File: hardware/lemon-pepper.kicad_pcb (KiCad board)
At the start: 4 copper layers, 35 x 35 mm, 90 parts, among them J101 INPUT, J201 USB_C_Receptacle_USB2.0, J301 TagConnect, J302 USER CONN., M101 MOT, Q501 MMBT5551, SW301 USER, U201 SRV05-4, U301 STM32G431, U302 SN65HVD230, U401 MT6835, U501 MAX15062CATA+T, U601 L6226QTR, U701 MAX49925, U703 MAX49925, Y301 12MHz

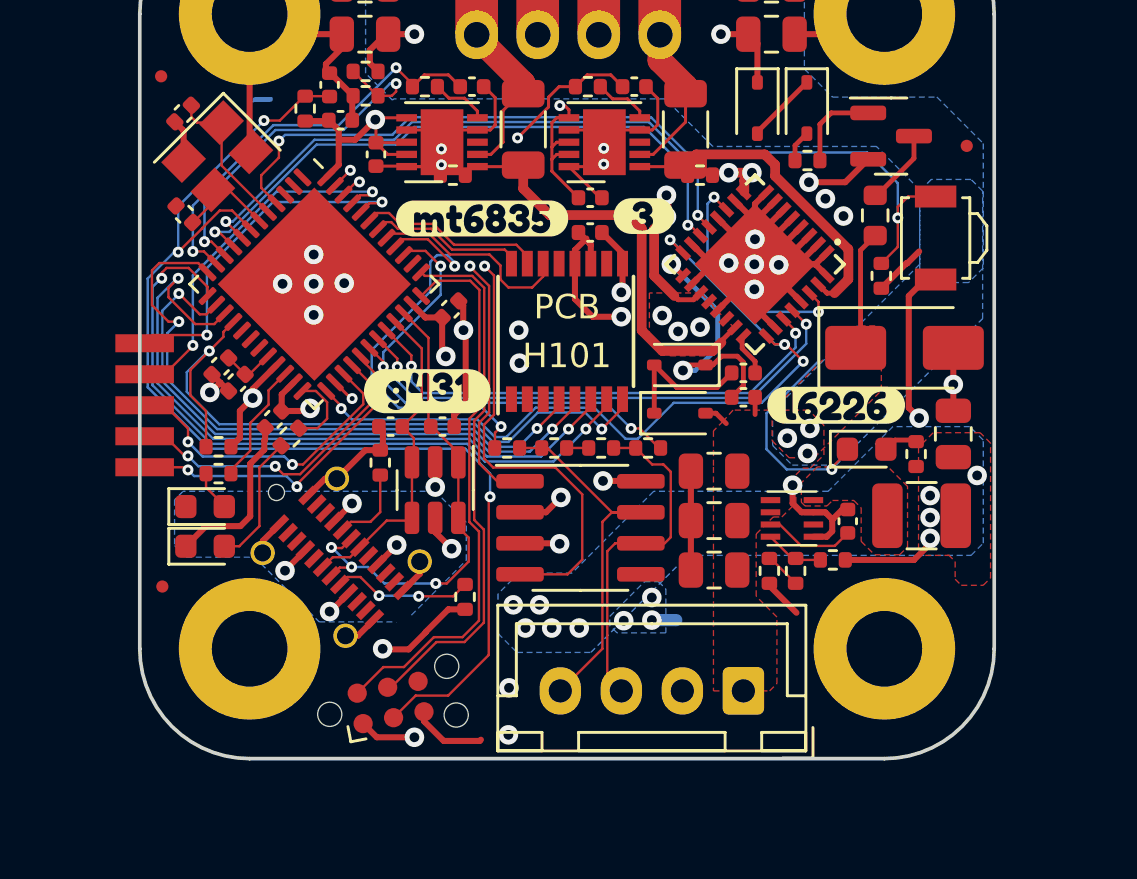
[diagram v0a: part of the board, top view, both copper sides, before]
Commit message: change inductor footprint, add I2C1 SCL on user 3
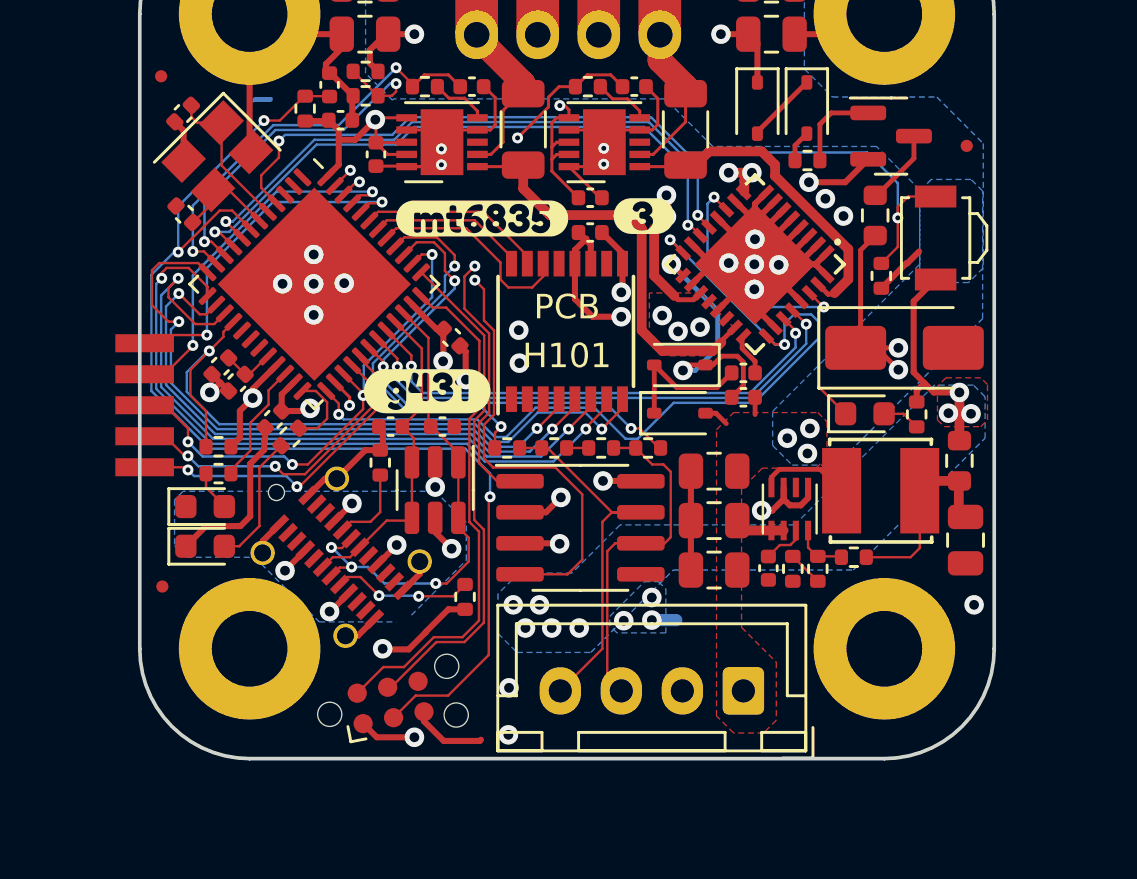
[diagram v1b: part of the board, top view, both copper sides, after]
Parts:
- removed the R701 at (141.6, 80.6)
- removed the R702 at (151.8, 80.6)
- removed kibuzzard-65305A5A: G***, kibuzzard-65305A5A
- added R506: 0R, Resistor_SMD:R_0603_1608Metric, F.Cu at (162.4, 92.3)
- L501: footprint Inductor_SMD:L_1210_3225Metric -> easyeda2kicad:IND-SMD_L4.0-W4.0
- R501: value 200k -> 0R
- U501: value MAX15062CATA+T -> MAX15062AATA+T
- moved C503 4.38 mm to (162.6, 95.5), turned to -90 degrees
- moved C502 3.78 mm to (154.6, 96.7), turned to -90 degrees
- moved L501 1.96 mm to (159.2, 93.5)
- moved R601 1.63 mm to (160.6, 90.4), turned to 90 degrees
- moved D601 1.45 mm to (158.5, 90.3)
- moved C304 1.16 mm to (141.6, 87.2), turned to -45 degrees
- moved R503 0.96 mm to (155.6, 96.7)
- moved R502 0.91 mm to (156.6, 96.7)
- moved R501 0.87 mm to (158.1, 96.2)
- moved U501 0.40 mm to (155.4, 94.2), turned to 0 degrees
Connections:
- net Net-(U301-PB10) renamed /mcu/LED_GOOD
- net Net-(U301-PB11) renamed /mcu/LED_FAULT
- C503 pad 1: +3V3 -> Net-(C503-Pad1)
- L501 pad 2: +3V3 -> Net-(C503-Pad1)
- R501 pad 1: +3V3 -> Net-(C503-Pad1)
- U301 pad 17: /current sense/W_SENSE -> unconnected-(U301-PB0-Pad17)
- U301 pad 38: unconnected-(U301-PA15-Pad38) -> /mcu/USER_3
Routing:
- net +3V3: track 66.8 -> 77.6 mm, vias 18 -> 16
- net GND: track 128.7 -> 118.9 mm
- net Net-(C503-Pad1): track 0.00 -> 8.09 mm
- net /mcu/USER_3: track 12.9 -> 20.9 mm, vias 2 -> 4
- net Vmot: track 18.6 -> 24.9 mm, vias 12 -> 14
- net Net-(D601-K): track 20.6 -> 15.0 mm, vias 3 -> 2
- net Net-(U501-LX): track 0.00 -> 3.79 mm
- net /half bridges/ENA: track 31.9 -> 35.3 mm, vias 4 -> 3
- net Net-(U501-VCC): track 3.75 -> 1.78 mm
- net /mcu/SWDIO: track 22.9 -> 21.2 mm
- net /mcu/DIR: track 21.0 -> 22.2 mm
- net /mcu/SWCLK: track 21.9 -> 20.8 mm
- net /mcu/STEP: track 17.3 -> 16.4 mm
- net /mcu/CAN_RX: track 26.3 -> 27.0 mm
- removed copper zone on F.Cu, net Net-(U501-LX)

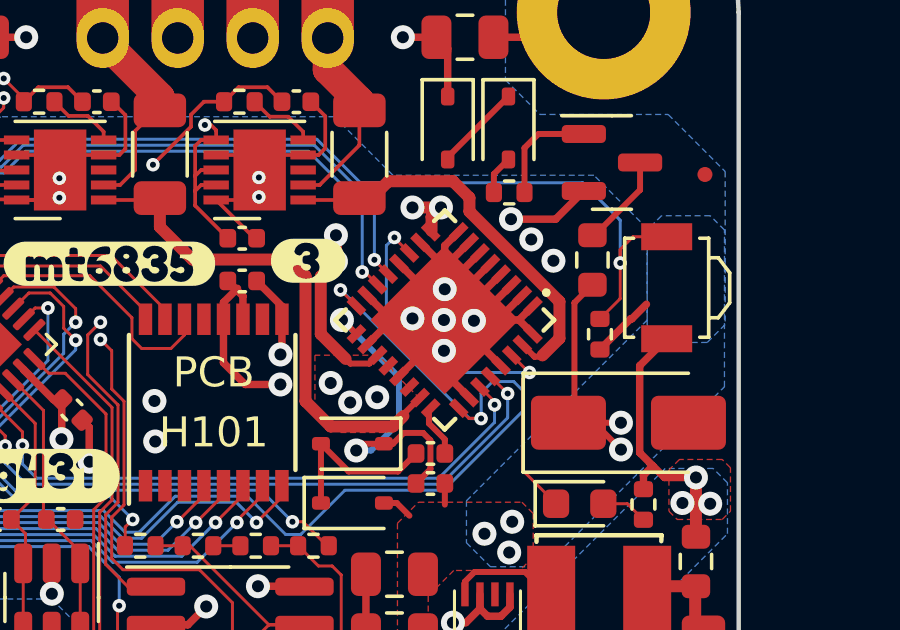
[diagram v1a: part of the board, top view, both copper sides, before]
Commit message: update L6226Q footprint and symbol
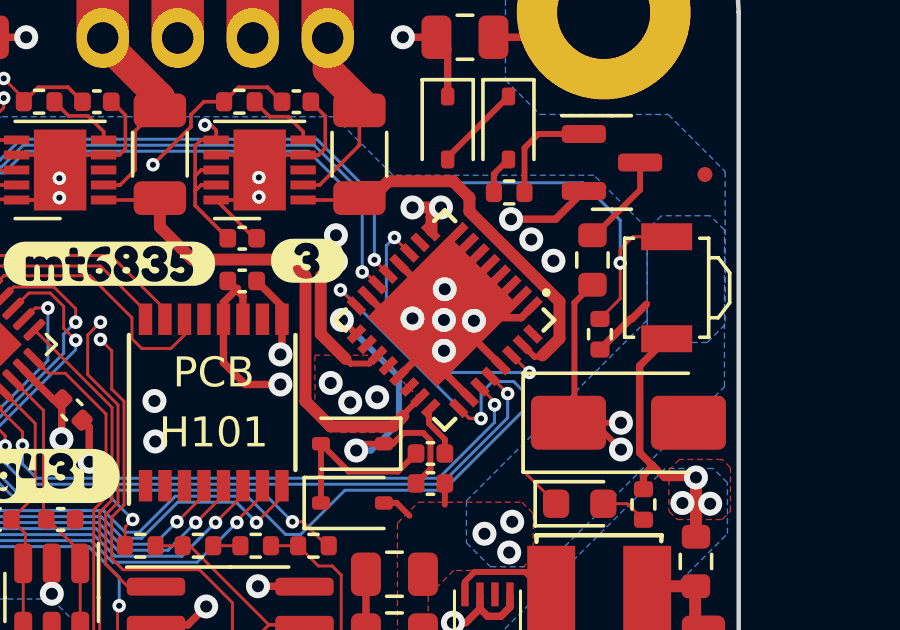
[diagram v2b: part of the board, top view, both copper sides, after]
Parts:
- U601: footprint easyeda2kicad:VQFN-32_L5.0-W5.0-P0.50-TL-EP -> matei:ST-L6226Q-VQFN32
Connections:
- U601 pad 10: GND -> unconnected-(U601-NC-Pad10)
- U601 pad 18: GND -> unconnected-(U601-NC-Pad18)
- U601 pad 32: GND -> unconnected-(U601-NC-Pad32)
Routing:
- net GND: track 118.9 -> 115.9 mm
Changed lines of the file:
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@@
   (net 86 "Net-(U703-OUT)")
   (net 87 "Net-(C503-Pad1)")
+  (net 88 "unconnected-(U601-NC-Pad10)")
+  (net 89 "unconnected-(U601-NC-Pad18)")
+  (net 90 "unconnected-(U601-NC-Pad32)")
   (footprint "Capacitor_SMD:C_0805_2012Metric" (layer "F.Cu")
     (at 138.025 74.8)
@@
     )
   )
-  (footprint "easyeda2kicad:VQFN-32_L5.0-W5.0-P0.50-TL-EP" (layer "F.Cu")
+  (footprint "matei:ST-L6226Q-VQFN32" (layer "F.Cu")
     (at 154 84.225 -135)
     (property "LCSC Part" "C95357")
@@
       (stroke (width 0.06) (type solid)) (fill none) (layer "F.Fab"))
     (pad "1" smd rect (at -2.41 -1.75 225) (size 0.66 0.28) (layers "F.Cu" "F.Paste" "F.Mask")
-      (net 1 "GND") (pinfunction "GND") (pintype "power_out"))
+      (net 1 "GND") (pinfunction "GND") (pintype "power_in"))
     (pad "2" smd rect (at -2.41 -1.25 225) (size 0.66 0.28) (layers "F.Cu" "F.Paste" "F.Mask")
       (net 1 "GND") (pinfunction "NC") (pintype "passive"))
@@
       (net 75 "/half bridges/OUT1B") (pinfunction "OUT1B") (pintype "output"))
     (pad "10" smd rect (at -1.25 2.41 225) (size 0.28 0.66) (layers "F.Cu" "F.Paste" "F.Mask")
-      (net 1 "GND") (pinfunction "NC") (pintype "passive"))
+      (net 88 "unconnected-(U601-NC-Pad10)") (pinfunction "NC") (pintype "no_connect"))
     (pad "11" smd rect (at -0.75 2.41 225) (size 0.28 0.66) (layers "F.Cu" "F.Paste" "F.Mask")
       (net 31 "Net-(D601-K)") (pinfunction "OCDB") (pintype "open_emitter"))
@@
       (net 30 "Net-(D603-K)") (pinfunction "VBOOT") (pintype "passive"))
     (pad "18" smd rect (at 2.41 1.25 225) (size 0.66 0.28) (layers "F.Cu" "F.Paste" "F.Mask")
-      (net 1 "GND") (pinfunction "NC") (pintype "passive"))
+      (net 89 "unconnected-(U601-NC-Pad18)") (pinfunction "NC") (pintype "no_connect"))
     (pad "19" smd rect (at 2.41 0.75 225) (size 0.66 0.28) (layers "F.Cu" "F.Paste" "F.Mask")
       (net 11 "/current sense/W_IN") (pinfunction "OUT2B") (pintype "output"))
@@
       (net 10 "/current sense/V_IN") (pinfunction "OUT1A") (pintype "output"))
     (pad "32" smd rect (at -1.75 -2.41 225) (size 0.28 0.66) (layers "F.Cu" "F.Paste" "F.Mask")
-      (net 1 "GND") (pinfunction "NC") (pintype "passive"))
-    (pad "33" smd rect (at 0 0 225) (size 3.5 3.5) (layers "F.Cu" "F.Paste" "F.Mask")
+      (net 90 "unconnected-(U601-NC-Pad32)") (pinfunction "NC") (pintype "no_connect"))
+    (pad "33" smd rect (at -0.165 0.25 225) (size 3.83 3.28) (layers "F.Cu" "F.Paste" "F.Mask")
       (net 1 "GND") (pinfunction "EP") (pintype "passive"))
     (model "/Users/mateijordache/Documents/KiCad/easyeda2kicad/easyeda2kicad.3dshapes/VQFN-32_L5.0-W5.0-H1.0-P0.50.wrl" hide
@@
     (pad "1" thru_hole circle locked (at 13 13) (size 5.8 5.8) (drill 3.1) (layers "*.Cu" "*.Mask")
       (net 1 "GND") (pinfunction "1") (pintype "input"))
-    (model "/Users/mateijordache/Documents/electronics_projects/lemon-pepper-stepper/mechanical/heatsink-nema-14.step" hide
-      (offset (xyz 0 0 0))
+    (model "/Users/mateijordache/Documents/electronics_projects/lemon-pepper-stepper/mechanical/heatsink-nema-14.step"
+      (offset (xyz 0 0 -1.5))
       (scale (xyz 1 1 1))
       (rotate (xyz 0 0 0))
@@
     (effects (font (size 1 1) (thickness 0.15)) (justify left bottom))
   )
+  (segment (start 156.549874 84.15) (end 155.55 84.15) (width 0.25) (layer "F.Cu") (net 1))
   (segment (start 152.575 84.225) (end 153.975 84.225) (width 0.25) (layer "F.Cu") (net 1))
   (segment (start 133.3 79.569365) (end 133.3 73.975) (width 0.25) (layer "F.Cu") (net 1))
@@
   (segment (start 133.935589 90.914411) (end 133.935589 91.402241) (width 0.25) (layer "F.Cu") (net 1))
   (segment (start 131.700879 89.474121) (end 132.098089 89.076911) (width 0.25) (layer "F.Cu") (net 1))
-  (segment (start 153.179756 81.636989) (end 154 82.457233) (width 0.25) (layer "F.Cu") (net 1))
   (segment (start 142.161 88.95) (end 142.15 88.939) (width 0.25) (layer "F.Cu") (net 1))
   (segment (start 155.875 94.1) (end 156.175 93.8) (width 0.25) (layer "F.Cu") (net 1))
@@
   (segment (start 142.775 103.7) (end 142.725 103.75) (width 0.25) (layer "F.Cu") (net 1))
   (segment (start 134.55 75.225) (end 133.3 73.975) (width 0.25) (layer "F.Cu") (net 1))
-  (segment (start 156.474874 84.225) (end 155.525 84.225) (width 0.25) (layer "F.Cu") (net 1))
   (segment (start 133.903482 91.816188) (end 133.325 92.39467) (width 0.25) (layer "F.Cu") (net 1))
   (segment (start 137.075 74.8) (end 134.125 74.8) (width 0.25) (layer "F.Cu") (net 1))
@@
   (segment (start 136.425 76.025) (end 136.425 76.175) (width 0.25) (layer "F.Cu") (net 1))
   (segment (start 155.475 84.225) (end 154 84.225) (width 0.25) (layer "F.Cu") (net 1))
-  (segment (start 151.411989 85.045244) (end 152.232233 84.225) (width 0.25) (layer "F.Cu") (net 1))
   (segment (start 154 82.625) (end 154 84.225) (width 0.25) (layer "F.Cu") (net 1))
   (segment (start 141.44 98.36) (end 140.518071 99.281929) (width 0.25) (layer "F.Cu") (net 1))
@@
   (segment (start 155.475 84.225) (end 155.45 84.25) (width 0.25) (layer "F.Cu") (net 1))
   (segment (start 154 82.725) (end 153.95 82.775) (width 0.25) (layer "F.Cu") (net 1))
-  (segment (start 155.5 84.2) (end 155.475 84.225) (width 0.25) (layer "F.Cu") (net 1))
   (segment (start 148.523639 86.374502) (end 147.349502 86.374502) (width 0.25) (layer "F.Cu") (net 1))
   (segment (start 156.234457 83.051203) (end 155.06066 84.225) (width 0.25) (layer "F.Cu") (net 1))
@@
   (segment (start 133.353858 79.623223) (end 133.3 79.569365) (width 0.25) (layer "F.Cu") (net 1))
   (segment (start 154.274136 94.313586) (end 154.706414 94.313586) (width 0.25) (layer "F.Cu") (net 1))
+  (segment (start 156.941564 83.75831) (end 156.549874 84.15) (width 0.25) (layer "F.Cu") (net 1))
   (segment (start 138.65 91.84) (end 138.040887 91.84) (width 0.25) (layer "F.Cu") (net 1))
   (segment (start 132.435589 89.414411) (end 132.098089 89.076911) (width 0.25) (layer "F.Cu") (net 1))
@@
   (segment (start 152.232233 84.225) (end 152.575 84.225) (width 0.25) (layer "F.Cu") (net 1))
   (segment (start 145.44 94.385) (end 144.375 94.385) (width 0.25) (layer "F.Cu") (net 1))
-  (segment (start 156.941564 83.75831) (end 156.474874 84.225) (width 0.25) (layer "F.Cu") (net 1))
   (segment (start 154.820244 86.813011) (end 154.032233 86.025) (width 0.25) (layer "F.Cu") (net 1))
   (segment (start 158.075 72.75) (end 159.3 73.975) (width 0.25) (layer "F.Cu") (net 1))
+  (segment (start 155.55 84.15) (end 155.475 84.225) (width 0.25) (layer "F.Cu") (net 1))
   (segment (start 135.702639 93.694187) (end 136.388533 93.008293) (width 0.25) (layer "F.Cu") (net 1))
   (segment (start 154 83.16434) (end 154 84.225) (width 0.25) (layer "F.Cu") (net 1))
@@
   (segment (start 151.375 94.725) (end 151.375 96.75) (width 0.25) (layer "F.Cu") (net 1))
   (segment (start 137.075 74.8) (end 137.075 75.375) (width 0.25) (layer "F.Cu") (net 1))
-  (segment (start 155.525 84.225) (end 155.5 84.2) (width 0.25) (layer "F.Cu") (net 1))
   (segment (start 140.9 93.3459) (end 140.9 92.3375) (width 0.25) (layer "F.Cu") (net 1))
   (segment (start 132.098089 89.076911) (end 131.760589 88.739411) (width 0.25) (layer "F.Cu") (net 1))
   (segment (start 146.77 82.925) (end 147.275 83.43) (width 0.25) (layer "F.Cu") (net 1))
   (segment (start 146.05 93.775) (end 145.44 94.385) (width 0.25) (layer "F.Cu") (net 1))
-  (segment (start 156.941564 84.69169) (end 156.474874 84.225) (width 0.25) (layer "F.Cu") (net 1))
   (segment (start 131.5125 94.95) (end 130.6875 95.775) (width 0.25) (layer "F.Cu") (net 1))
   (segment (start 142.125 98.36) (end 141.44 98.36) (width 0.25) (layer "F.Cu") (net 1))

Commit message: v3 fixes, appropriate inductor
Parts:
- removed kibuzzard-6547C3FC: G***, kibuzzard-6547C3FC
- added kibuzzard-65A1D30A: G***, kibuzzard-65A1D30A, F.Cu at (162.4, 77.4)
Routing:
- net /half bridges/ENA: track 35.3 -> 36.1 mm
- net /half bridges/IN2A: track 21.6 -> 22.2 mm
- net Net-(D601-K): track 15.0 -> 15.5 mm
- net /half bridges/IN1A: track 20.6 -> 21.1 mm
- net GND: track 115.9 -> 115.8 mm, vias 26 -> 24

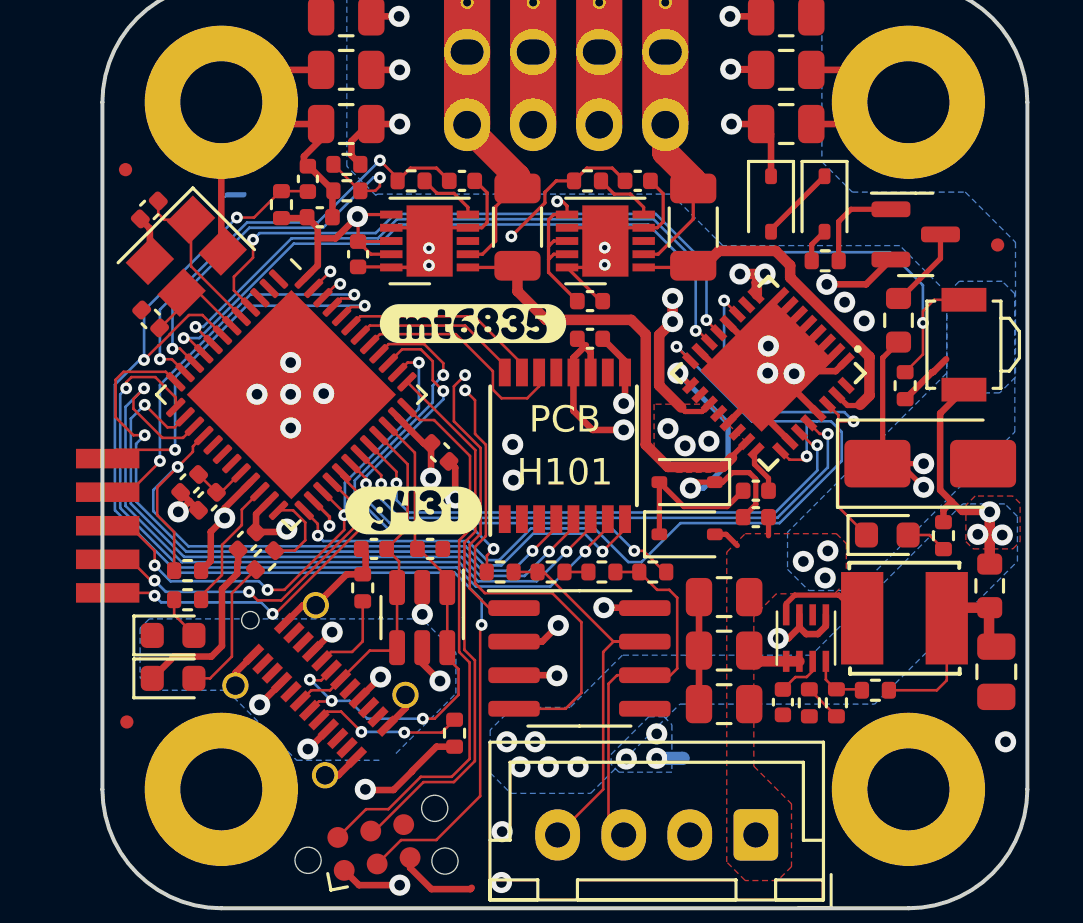
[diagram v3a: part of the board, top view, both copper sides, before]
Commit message: Made analog gain of current sense amps selectable by mcu. Removed analog ground plane and tied all grounds together
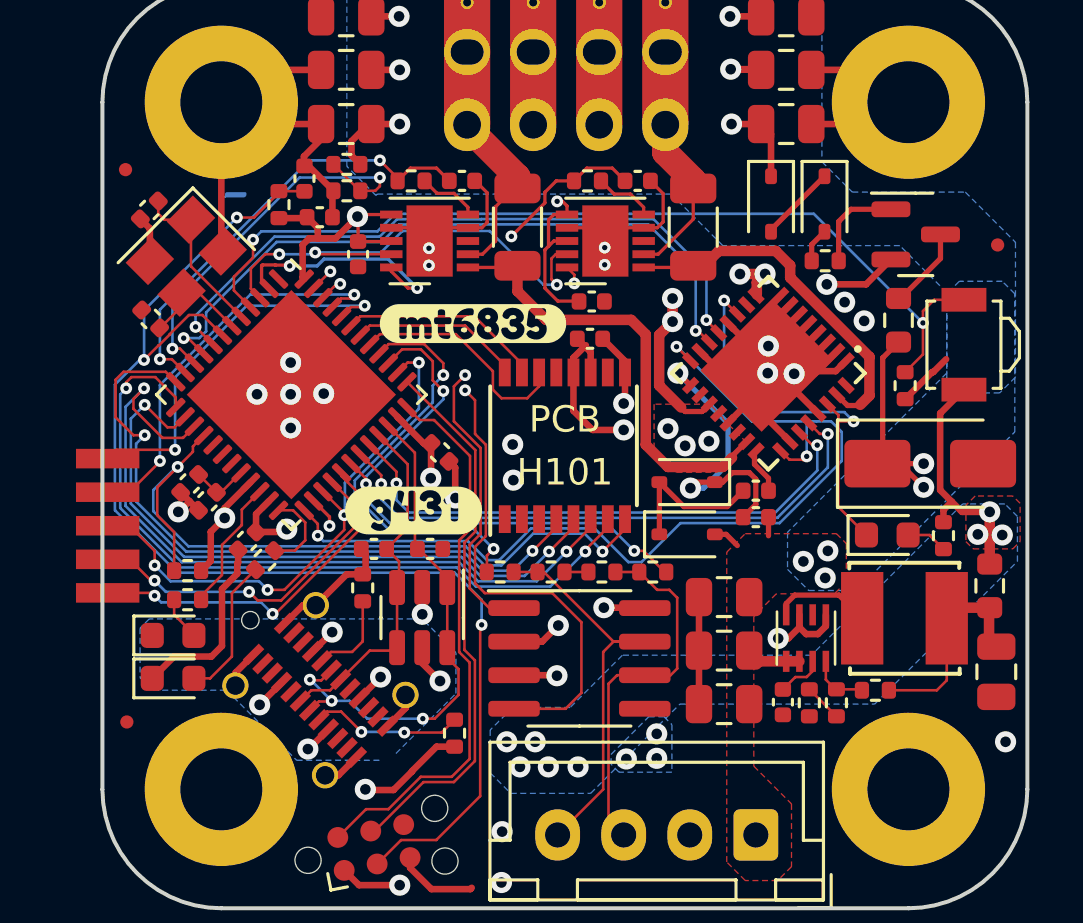
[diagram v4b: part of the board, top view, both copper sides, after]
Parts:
- removed NT701: NetTie_2, NetTie:NetTie-2_SMD_Pad0.5mm
- moved C308 0.13 mm to (136.4, 76.9)
- moved R306 0.10 mm to (135.5, 77.8)
- moved C703 0.07 mm to (147.3, 81.5)
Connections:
- C701 pad 2: GNDA -> GND
- C702 pad 2: GNDA -> GND
- C703 pad 2: GNDA -> GND
- C704 pad 2: GNDA -> GND
- U301 pad 2: unconnected-(U301-PC13-Pad2) -> /current sense/GAIN_0
- U301 pad 3: unconnected-(U301-PC14-Pad3) -> /current sense/GAIN_1
- U701 pad 10: GNDA -> /current sense/GAIN_0
- U701 pad 11: GNDA -> GND
- U701 pad 4: GNDA -> GND
- U701 pad 7: GNDA -> GND
- U701 pad 9: +3V3 -> /current sense/GAIN_1
- U703 pad 10: GNDA -> /current sense/GAIN_0
- U703 pad 11: GNDA -> GND
- U703 pad 4: GNDA -> GND
- U703 pad 7: GNDA -> GND
- U703 pad 9: +3V3 -> /current sense/GAIN_1
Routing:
- net GNDA: track 21.4 -> 0.00 mm, vias 7 -> 0
- net /current sense/GAIN_1: track 0.00 -> 19.0 mm, vias 0 -> 3
- net /current sense/GAIN_0: track 0.00 -> 18.9 mm, vias 0 -> 3
- net GND: track 115.8 -> 130.4 mm, vias 24 -> 31
- net +3V3: track 77.6 -> 76.2 mm
- net /mcu/USER_BTN: track 35.7 -> 34.9 mm
- added copper zone on B.Cu, net Net-(NT701-Pad1)
- removed copper zone on B.Cu, net GNDA
- removed copper zone on In1.Cu, net GNDA

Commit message: get DRC clean
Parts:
- moved R703 0.16 mm to (151.3, 78.7)
- moved U703 0.14 mm to (148.0, 79.2)
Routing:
- net /mcu/ADC1_IN12: track 15.1 -> 17.9 mm
- net GND: track 130.4 -> 132.8 mm, vias 31 -> 32
- net +3V3: track 76.2 -> 74.8 mm, vias 16 -> 17
- net /half bridges/IN1B: track 25.5 -> 26.3 mm
- net /half bridges/IN2B: track 26.2 -> 27.0 mm
- net /mcu/USER_BTN: track 34.9 -> 35.6 mm
- net /current sense/V_SENSE: track 27.6 -> 27.0 mm
- net /current sense/GAIN_1: track 19.0 -> 18.9 mm, vias 3 -> 2
